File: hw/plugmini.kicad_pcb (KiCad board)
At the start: 4 copper layers, 48 x 64 mm, 46 parts, among them J1 AudioJackMono4p, J2 AudioJackStereo, P1 CONN_02X05, U1 tlv320aic3120, U2 ATSAM4LS, U4 LME49721, Y1 16MHz

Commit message: Layout updates
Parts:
- added D1: PRTR5V0U2X, comm:SOT143B, F.Cu at (128.7, 106.7)
- added J3: MicroSDCard, processing:sdcard_pushpull, F.Cu at (121.0, 80.2)
- added P2: USB_OTG, Connect:USB_Micro-B, F.Cu at (129.2, 119.6)
- added R12, R15: 10k, Resistors_SMD:R_0603, F.Cu at (144.0, 134.1)
- C1, C10, C11, C12, C13, C14, C15, C17, C3, C6, C8: footprint Resistors_SMD:R_0603 -> Resistors_SMD:R_0402
- L1: value 22uH -> ferrite
- moved C12 103.7 mm to (140.3, 100.9), turned to 90 degrees
- moved C13 102.8 mm to (141.8, 95.6)
- moved C16 102.4 mm to (136.3, 105.5)
- moved C15 101.2 mm to (135.9, 103.6)
- moved L2 100.5 mm to (136.1, 101.7)
- moved C10 99.9 mm to (140.8, 90.6)
- moved R1 98.3 mm to (133.5, 102.1), turned to 90 degrees
- moved Y1 95.8 mm to (123.1, 102.3), turned to 90 degrees
- moved C17 95.7 mm to (143.3, 63.4)
- moved C14 92.3 mm to (138.6, 71.8)
- moved C8 91.7 mm to (138.7, 68.1)
- moved C6 91.3 mm to (138.8, 64.8)
- moved C3 90.8 mm to (138.5, 62.3)
- moved C11 90.6 mm to (129.1, 93.9), turned to 180 degrees
- moved L1 88.3 mm to (134.3, 73.0)
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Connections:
- U2 pad 36: Net-(U2-Pad36) -> /Processor/~SS
- U2 pad 37: Net-(U2-Pad37) -> /Processor/SPI_CLK
- U2 pad 38: Net-(U2-Pad38) -> /Processor/MISO
- U2 pad 39: Net-(U2-Pad39) -> /Processor/MOSI
- U2 pad 46: Net-(U2-Pad46) -> /Processor/D-
- U2 pad 47: Net-(U2-Pad47) -> /Processor/D+
- U2 pad 49: (no net) -> GND
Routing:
- net /Processor/MISO: track 0.00 -> 20.6 mm, vias 0 -> 2
- net /Processor/SPI_CLK: track 0.00 -> 18.3 mm
- net GND: track 6.70 -> 24.2 mm, vias 6 -> 22
- net /Processor/MOSI: track 0.00 -> 16.3 mm
- net /Processor/~SS: track 0.00 -> 14.2 mm, vias 0 -> 2
- net /Processor/ISMK: track 0.00 -> 12.7 mm
- net /Sheet57346997/DOUT: track 0.00 -> 12.5 mm, vias 0 -> 2
- net /Processor/ISWS: track 0.00 -> 11.4 mm, vias 0 -> 2
- net VDD: track 0.00 -> 10.9 mm, vias 0 -> 8
- net /Sheet57346997/DIN: track 0.00 -> 10.8 mm, vias 0 -> 2
- net /Sheet57346997/BCLK: track 0.00 -> 8.85 mm, vias 0 -> 2
- net /Processor/VDDCORE: track 0.00 -> 6.93 mm
- net /Processor/D-: track 0.00 -> 3.44 mm
- net Net-(L2-Pad2): track 0.00 -> 3.33 mm
- net /Processor/D+: track 0.00 -> 3.26 mm
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- added copper zone on F.Cu, net GND
- added copper zone on In2.Cu, net VDD

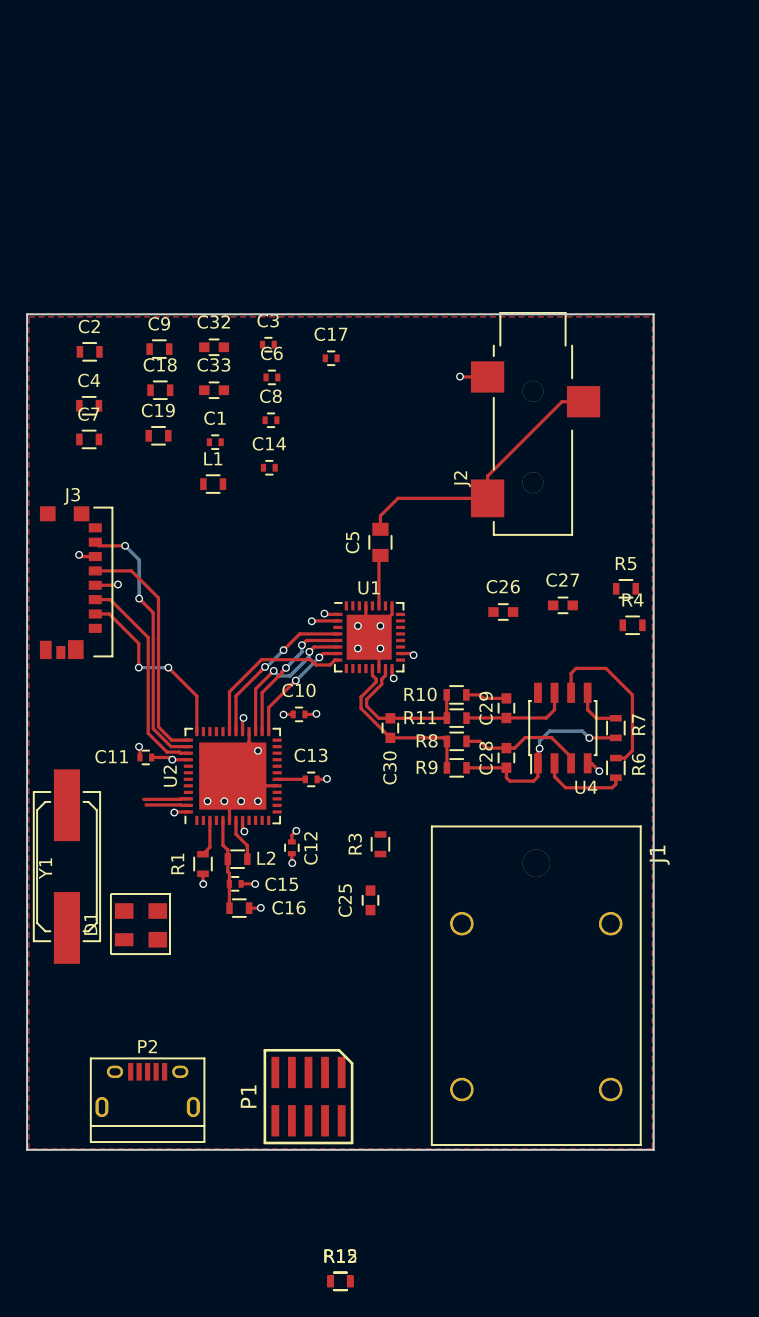
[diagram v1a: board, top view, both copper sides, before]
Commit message: Version 0.1. No BLE, no cap touch and 4 layers
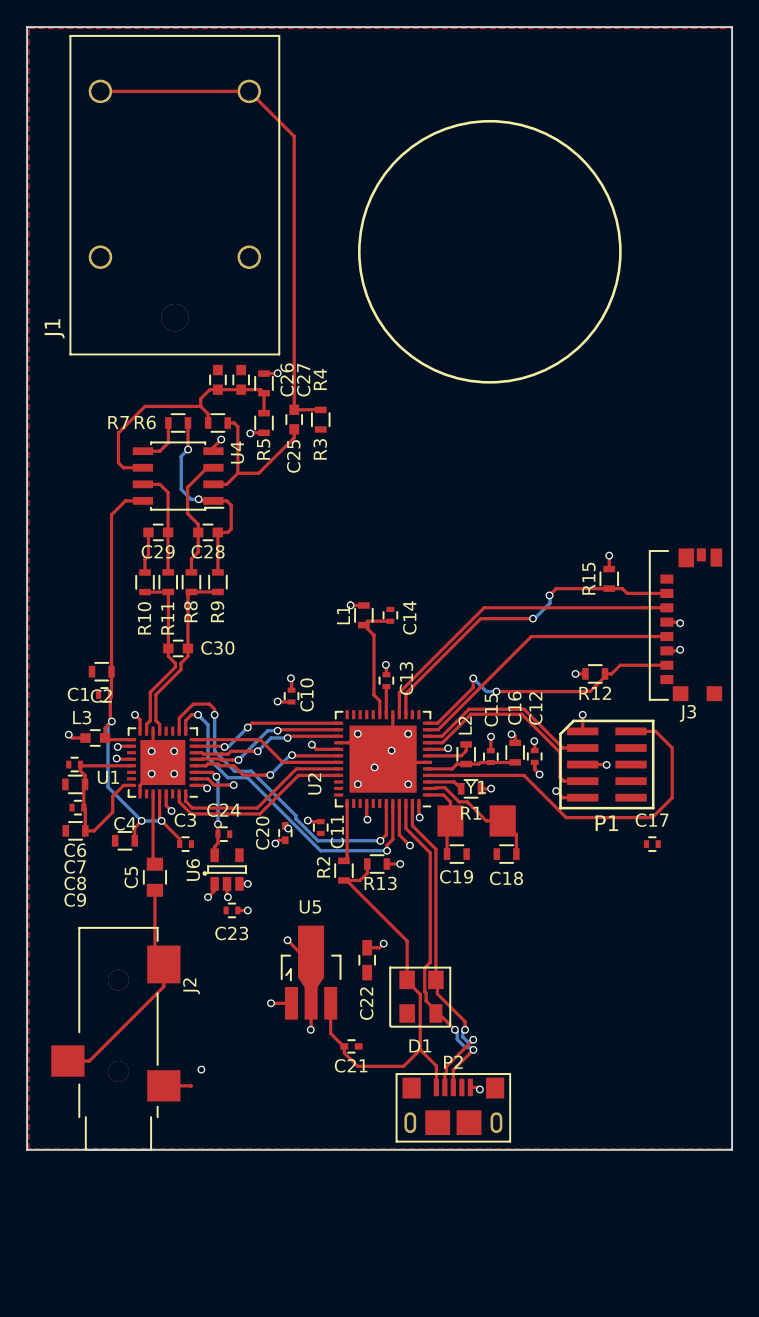
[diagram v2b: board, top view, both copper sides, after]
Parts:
- removed C32, C33: 1uF, Capacitors_SMD:C_0603
- added C20: 0.1u, Capacitors_SMD:C_0402, F.Cu at (139.8, 99.7)
- added C21: 0.1u, Capacitors_SMD:C_0402, F.Cu at (144.8, 116.1)
- added C22: 10u, Capacitors_SMD:C_0603_HandSoldering, F.Cu at (146.1, 109.5)
- added C23: 0.1uF, Resistors_SMD:R_0402, F.Cu at (135.7, 105.7)
- added C24: 0.1uF, Resistors_SMD:R_0402, F.Cu at (135.1, 99.8)
- added L3: L_Small, Capacitors_SMD:C_0603, F.Cu at (125.2, 92.5)
- added R13: 1M, Resistors_SMD:R_0603, F.Cu at (146.8, 102.1)
- added R2: 820k, Resistors_SMD:R_0603, F.Cu at (144.3, 102.6)
- added U5: AZ1117C, Housings_SOT-89:SOT89-3_Housing_Handsoldering, F.Cu at (141.8, 110.4)
- added U6: TLV71318, Housings_SOT-23_SOT-143_TSOT-6:SOT-23-5, F.Cu at (135.3, 102.5)
- P2: footprint Connect:USB_Micro-B -> processing:USB_Micro-B101181930001LF
- Y1: footprint Crystals_Oscillators_SMD:Q_49U3HMS -> processing:2SMD
- moved J1 69.5 mm to (131.3, 49.3), turned to 90 degrees
- moved R15 57.6 mm to (164.6, 80.3), turned to 270 degrees
- moved J3 52.4 mm to (173.2, 84.1), turned to 90 degrees
- moved R12 50.5 mm to (163.5, 87.5)
- moved J2 49.6 mm to (127.0, 111.0), turned to 90 degrees
- moved C17 44.6 mm to (167.9, 100.6)
- moved C18 44.3 mm to (156.7, 101.3), turned to 180 degrees
- moved R7 40.9 mm to (131.6, 68.3), turned to 180 degrees
- moved R6 40.3 mm to (134.6, 68.3), turned to 0 degrees
- moved C19 39.4 mm to (152.9, 101.3)
- moved C3 38.8 mm to (132.1, 100.6)
- moved C9 37.5 mm to (123.7, 99.6), turned to 180 degrees
- moved C25 37.3 mm to (140.5, 68.1)
- moved U4 35.2 mm to (131.6, 72.4), turned to 180 degrees
- moved P1 34.2 mm to (164.4, 94.5), turned to 0 degrees
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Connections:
- C1 pad 1: VAA -> +3.3VDAC
- C2 pad 1: VAA -> +3.3VDAC
- C3 pad 1: VAA -> +3.3VDAC
- C4 pad 1: VAA -> +3.3VDAC
- C6 pad 2: GNDA -> GND
- C7 pad 2: GNDA -> GND
- C8 pad 2: GNDA -> GND
- C9 pad 2: GNDA -> GND
- D1 pad 4: /USB/VBUS -> VCC
- P2 pad 1: /USB/VBUS -> VCC
- U1 pad 10: /Sheet57346997/SCL -> /Processor/SCL
- U1 pad 17: VAA -> +3.3VDAC
- U1 pad 28: VAA -> +3.3VDAC
- U1 pad 31: /Sheet57346997/~CODEC_RESET -> /Processor/CODEC_RST
- U1 pad 32: /Sheet57346997/CODEC_IO -> /Processor/CODEC_IO
- U1 pad 9: /Sheet57346997/SDA -> /Processor/SDA
- U2 pad 11: Net-(U2-Pad11) -> /Processor/SPI_CLK
- U2 pad 12: Net-(U2-Pad12) -> /Processor/MISO
- U2 pad 15: Net-(U2-Pad15) -> /Processor/~SS
- U2 pad 16: Net-(U2-Pad16) -> /Processor/MOSI
- U2 pad 32: Net-(U2-Pad32) -> /Processor/CODEC_IO
- U2 pad 33: Net-(U2-Pad33) -> /Processor/CODEC_RST
- U2 pad 36: /Processor/~SS -> Net-(U2-Pad36)
- U2 pad 37: /Processor/SPI_CLK -> Net-(R2-Pad1)
- U2 pad 38: /Processor/MISO -> Net-(U2-Pad38)
- U2 pad 39: /Processor/MOSI -> Net-(U2-Pad39)
- U2 pad 43: Net-(U2-Pad43) -> /Processor/SCL
- U2 pad 44: Net-(U2-Pad44) -> /Processor/SDA
- U4 pad 8: VAA -> +3.3VDAC
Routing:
- net Net-(C25-Pad2): track 0.00 -> 39.2 mm
- net +3.3VDAC: track 0.00 -> 38.9 mm, vias 0 -> 3
- net VCC: track 0.00 -> 32.7 mm
- net /Processor/~RESET: track 0.00 -> 28.2 mm
- net /Processor/SCL: track 0.00 -> 26.3 mm, vias 0 -> 2
- net /Processor/SDA: track 0.00 -> 26.0 mm, vias 0 -> 2
- net /Processor/D+: track 3.26 -> 25.2 mm, vias 0 -> 2
- net /Processor/D-: track 3.44 -> 25.3 mm, vias 0 -> 2
- net VDD: track 10.9 -> 32.3 mm, vias 8 -> 23
- net GND: track 24.2 -> 41.3 mm, vias 22 -> 31
- net /Processor/SWD_CLK: track 0.00 -> 16.0 mm
- net /Sheet57346997/SPKVDD: track 0.00 -> 15.0 mm
- net /Processor/CODEC_RST: track 0.00 -> 14.4 mm
- net /Processor/SWD_DIO: track 0.00 -> 14.0 mm
- net /Processor/CODEC_IO: track 0.00 -> 13.7 mm
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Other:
- board size 48 x 64 mm -> 54 x 86 mm

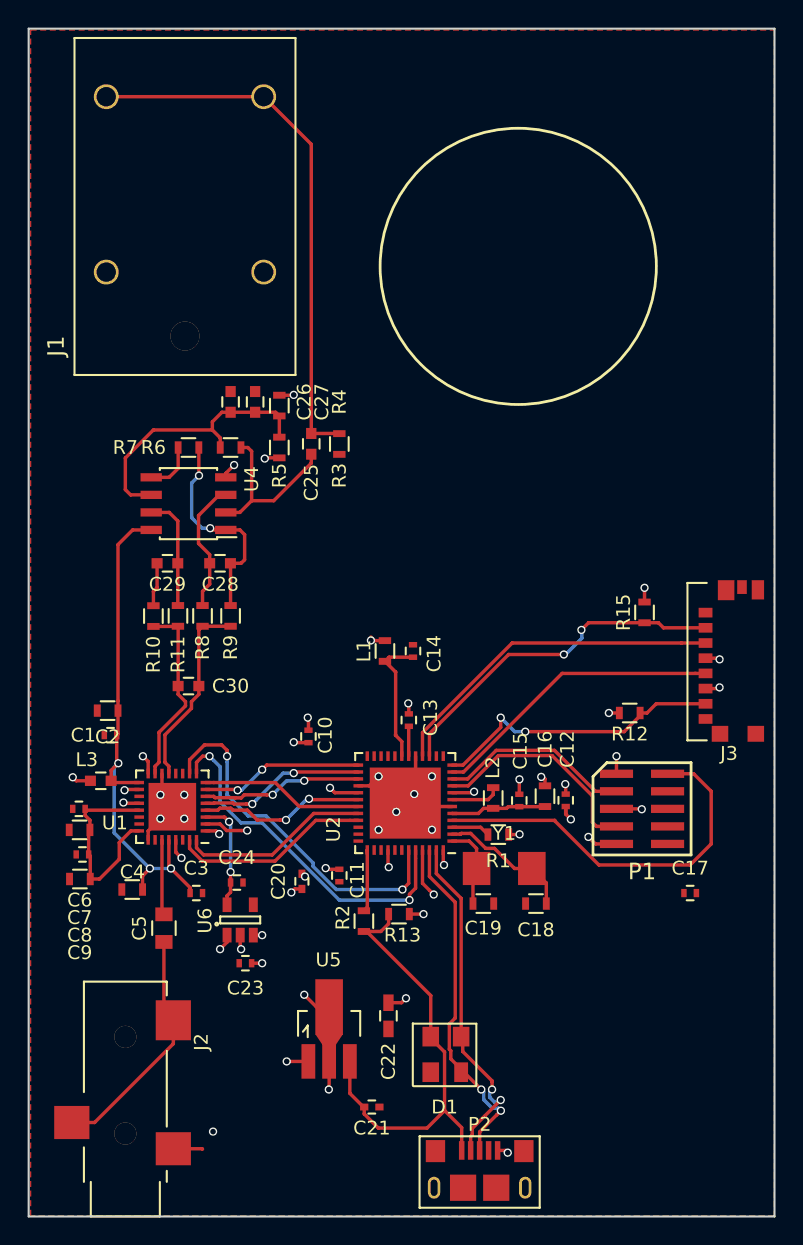
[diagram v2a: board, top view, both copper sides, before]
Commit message: Added few leds and cap pads
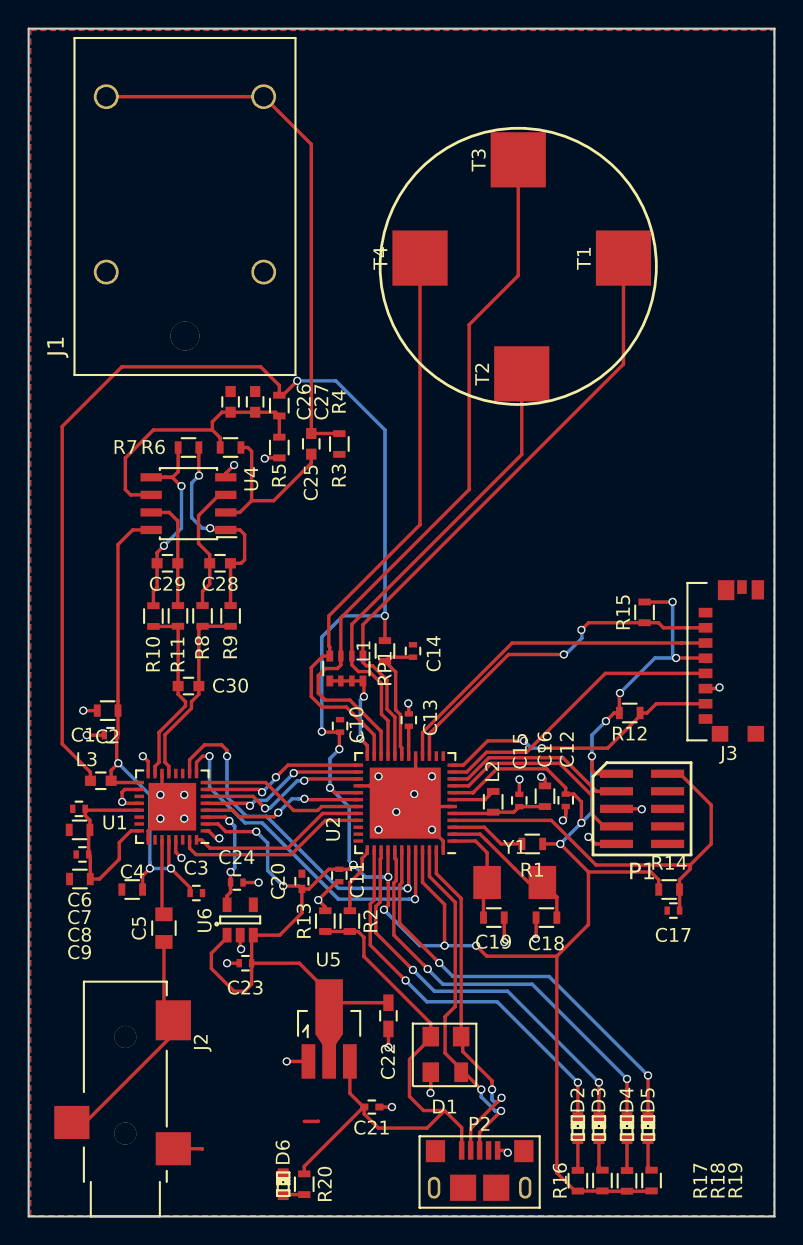
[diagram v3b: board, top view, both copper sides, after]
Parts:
- added D2: Led_Small, LEDs:LED-0603, F.Cu at (159.8, 117.6)
- added D3: Led_Small, LEDs:LED-0603, F.Cu at (161.3, 117.6)
- added D4: Led_Small, LEDs:LED-0603, F.Cu at (163.3, 117.6)
- added D5: Led_Small, LEDs:LED-0603, F.Cu at (164.8, 117.6)
- added D6: Led_Small, LEDs:LED-0603, F.Cu at (138.4, 121.7)
- added R14: 1k, Resistors_SMD:R_0603, F.Cu at (166.4, 100.3)
- added R16: 1k, Resistors_SMD:R_0603, F.Cu at (159.8, 121.4)
- added R17: 1k, Resistors_SMD:R_0603, F.Cu at (161.5, 121.4)
- added R18: 1k, Resistors_SMD:R_0603, F.Cu at (163.3, 121.4)
- added R19: 1k, Resistors_SMD:R_0603, F.Cu at (165.1, 121.4)
- added R20: 1k, Resistors_SMD:R_0603, F.Cu at (140.0, 121.7)
- added RP1: R_PACK4, Resistors_SMD:R_Array_Convex_4x0603, F.Cu at (143.0, 84.3)
- added T1: touchkey, processing:touchkey, F.Cu at (163.1, 54.6)
- added T2: touchkey, processing:touchkey, F.Cu at (155.7, 63.0)
- added T3: touchkey, processing:touchkey, F.Cu at (155.4, 47.5)
- added T4: touchkey, processing:touchkey, F.Cu at (148.3, 54.6)
- moved R13 5.36 mm to (141.5, 102.6), turned to 90 degrees
- moved R1 2.55 mm to (156.5, 97.0)
- moved C10 2.41 mm to (142.5, 88.5)
- moved C17 1.76 mm to (166.7, 101.9), turned to 180 degrees
- moved Y1 1.27 mm to (155.2, 99.8)
- moved C18 1.27 mm to (157.5, 102.4)
- moved C19 1.27 mm to (153.7, 102.4)
- moved R2 1.02 mm to (143.3, 102.6)
- moved L2 0.28 mm to (153.6, 94.0)
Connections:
- C17 pad 1: Net-(C17-Pad1) -> /Processor/~RESET
- C17 pad 2: Net-(C17-Pad2) -> GND
- U2 pad 20: Net-(U2-Pad20) -> /Processor/CATB4
- U2 pad 21: Net-(U2-Pad21) -> /Processor/CATB5
- U2 pad 22: Net-(U2-Pad22) -> /Processor/CATB6
- U2 pad 23: Net-(U2-Pad23) -> /Processor/CATB7
- U2 pad 24: Net-(U2-Pad24) -> /CapacitiveUI/DIS
- U2 pad 38: Net-(U2-Pad38) -> /Processor/LED0
- U2 pad 39: Net-(U2-Pad39) -> /Processor/LED1
- U2 pad 41: Net-(U2-Pad41) -> /Processor/LED2
- U2 pad 42: Net-(U2-Pad42) -> /Processor/LED3
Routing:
- net VDD: track 32.3 -> 256.0 mm, vias 23 -> 20
- net /Processor/CATB6: track 0.00 -> 52.6 mm
- net /Processor/CATB4: track 0.00 -> 45.1 mm
- net /Processor/CATB7: track 0.00 -> 42.6 mm
- net /Processor/CATB5: track 0.00 -> 34.3 mm
- net /Processor/LED3: track 0.00 -> 31.0 mm, vias 0 -> 2
- net /Processor/LED2: track 0.00 -> 30.3 mm, vias 0 -> 2
- net /Processor/LED1: track 0.00 -> 29.3 mm, vias 0 -> 2
- net /Processor/LED0: track 0.00 -> 28.7 mm, vias 0 -> 2
- net GND: track 41.3 -> 55.4 mm, vias 31 -> 36
- net Net-(C29-Pad1): track 6.91 -> 15.8 mm, vias 0 -> 2
- net VCC: track 32.7 -> 41.3 mm
- net /CapacitiveUI/DIS: track 0.00 -> 8.18 mm, vias 0 -> 2
- net /Processor/~RESET: track 28.2 -> 31.3 mm
- net Net-(R1-Pad2): track 2.81 -> 5.55 mm
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- added copper zone on B.Cu, net GND
- removed copper zone on In1.Cu, net GND
- removed copper zone on In2.Cu, net VDD
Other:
- copper layers 4 -> 2
- net class Default: clearance 0.13 -> 0.1524
- rule trace_clearance: 0.13 -> 0.1524
